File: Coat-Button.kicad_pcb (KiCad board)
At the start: 2 copper layers, 18 x 18 mm, 24 parts, among them IC1 MADW__ATTINY13-MM, P1 CONN_1, P2 CONN_1, P3 CONN_1, P4 CONN_1

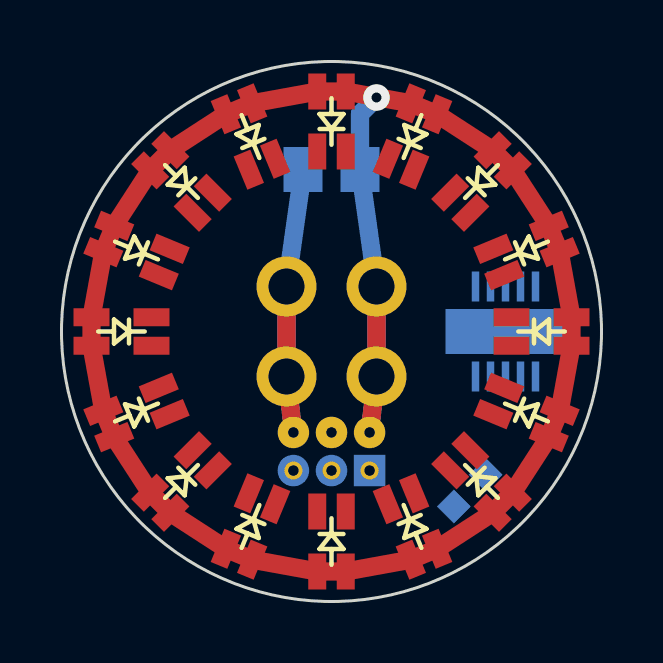
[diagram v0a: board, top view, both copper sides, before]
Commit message: On-board ATtiny13 wasn't doable. Not enough space.
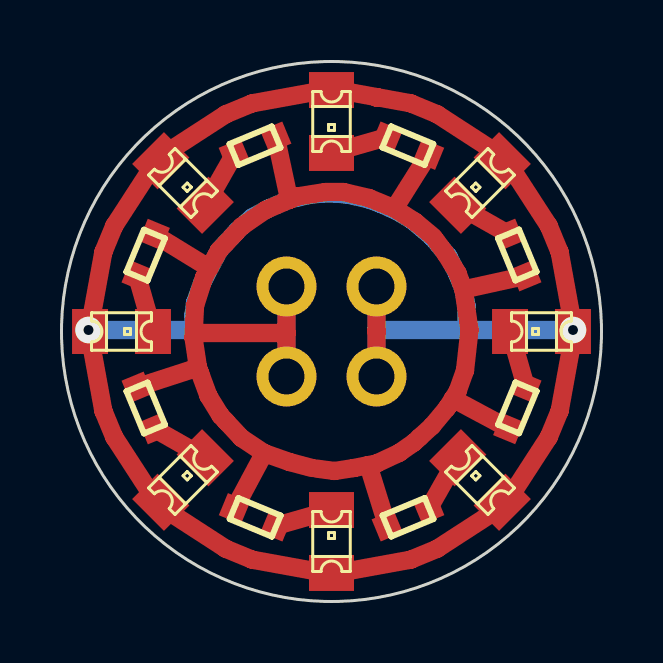
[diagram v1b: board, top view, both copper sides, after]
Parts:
- removed C1: 4.7µF, MADW__C0805
- removed IC1: MADW__ATTINY13-MM, MADW__MLF10
- removed JP1: AVR_ISP, MADW__PIN_ARRAY_3x2_1.27mm
- removed LED_A1_1, LED_A1_2, LED_A1_3, LED_A1_4, LED_A1_5, LED_A2_1, LED_A2_2, LED_A2_3, LED_A2_4, LED_A2_5, LED_B1_1, LED_B1_2, LED_B1_3, LED_B2_1, LED_B2_2, LED_B2_3: MADW__BI-LED, MADW__CHIPLED-0805-dual
- added D1: LED, MADW__CHIPLED-0805, F.Cu at (75.0, 55.0)
- added D2: LED, MADW__CHIPLED-0805, F.Cu at (75.0, 69.0)
- added D3: LED, MADW__CHIPLED-0805, F.Cu at (82.0, 62.0)
- added D4: LED, MADW__CHIPLED-0805, F.Cu at (68.0, 62.0)
- added D5: LED, MADW__CHIPLED-0805, F.Cu at (80.0, 57.0)
- added D6: LED, MADW__CHIPLED-0805, F.Cu at (80.0, 67.0)
- added D7: LED, MADW__CHIPLED-0805, F.Cu at (70.0, 67.0)
- added D8: LED, MADW__CHIPLED-0805, F.Cu at (70.0, 57.0)
- added G***: LED_smile_silkscreen_5mm, LED_smile_silkscreen_5mm, B.Cu at (75.0, 56.4)
- added G***: OSHW-logo_silkscreen_5mm, OSHW-logo_silkscreen_5mm, B.Cu at (75.0, 68.1)
- added R2: R, MADW__R0603, F.Cu at (72.5, 68.2)
- added R3: R, MADW__R0603, F.Cu at (81.2, 64.5)
- added R4: R, MADW__R0603, F.Cu at (68.8, 59.5)
- added R5: R, MADW__R0603, F.Cu at (81.2, 59.5)
- added R6: R, MADW__R0603, F.Cu at (77.5, 68.2)
- added R7: R, MADW__R0603, F.Cu at (68.8, 64.5)
- added R8: R, MADW__R0603, F.Cu at (72.5, 55.8)
- P1, P2, P4: footprint 1pin -> MADW__SIL-1
- R1: value 10k -> R; moved to F.Cu
- moved R1 11.7 mm to (77.5, 55.8), turned to 157.5 degrees
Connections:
- R1 pad 1: /RST -> GND
- R1 pad 2: VCC -> N-000009
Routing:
- net GND: track 13.7 -> 55.2 mm
- net VCC: track 66.8 -> 81.0 mm, vias 1 -> 2
- net N-000008: track 0.00 -> 1.95 mm
- net N-000007: track 0.00 -> 1.95 mm
- net N-000006: track 0.00 -> 1.95 mm
- net N-000005: track 0.00 -> 1.95 mm
- net N-000009: track 0.00 -> 1.93 mm
- net N-000002: track 0.00 -> 1.93 mm
- net N-000004: track 0.00 -> 1.93 mm
- net N-000003: track 0.00 -> 1.93 mm
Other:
- net class Default: via_dia 0.889 -> 0.635
- net class LED added: clearance 0.1524, trace_width 0.3048, via_dia 0.635, via_drill 0.3302
- rule via_min_size: 0.889 -> 0.635
- board text added: "+"
- board text added: "-"
- board text added: "2013"
- board text added: "blog. spitzenpfeil.org"

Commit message: Added some stuff to the 'Driver-Board'.
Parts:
- R1, R2, R3, R4, R5, R6, R7, R8: value R -> 200
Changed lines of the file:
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@@
     (links 26)
     (no_connects 0)
-    (area 62.564285 52.949999 84.357142 71.050001)
+    (area 65.949999 52.949999 84.050001 71.050001)
     (thickness 1.6)
     (drawings 8)
@@
       (effects (font (size 1 1) (thickness 0.2)))
     )
-    (fp_text value R (at 0.01 1.61 157.5) (layer F.SilkS) hide
+    (fp_text value 200 (at 0.01 1.61 157.5) (layer F.SilkS) hide
       (effects (font (size 1 1) (thickness 0.2)))
     )
@@
       (effects (font (size 1 1) (thickness 0.2)))
     )
-    (fp_text value R (at 0.01 1.61 337.5) (layer F.SilkS) hide
+    (fp_text value 200 (at 0.01 1.61 337.5) (layer F.SilkS) hide
       (effects (font (size 1 1) (thickness 0.2)))
     )
@@
       (effects (font (size 1 1) (thickness 0.2)))
     )
-    (fp_text value R (at 0.01 1.61 67.5) (layer F.SilkS) hide
+    (fp_text value 200 (at 0.01 1.61 67.5) (layer F.SilkS) hide
       (effects (font (size 1 1) (thickness 0.2)))
     )
@@
       (effects (font (size 1 1) (thickness 0.2)))
     )
-    (fp_text value R (at 0.01 1.61 247.5) (layer F.SilkS) hide
+    (fp_text value 200 (at 0.01 1.61 247.5) (layer F.SilkS) hide
       (effects (font (size 1 1) (thickness 0.2)))
     )
@@
       (effects (font (size 1 1) (thickness 0.2)))
     )
-    (fp_text value R (at 0.01 1.61 112.5) (layer F.SilkS) hide
+    (fp_text value 200 (at 0.01 1.61 112.5) (layer F.SilkS) hide
       (effects (font (size 1 1) (thickness 0.2)))
     )
@@
       (effects (font (size 1 1) (thickness 0.2)))
     )
-    (fp_text value R (at 0.01 1.61 22.5) (layer F.SilkS) hide
+    (fp_text value 200 (at 0.01 1.61 22.5) (layer F.SilkS) hide
       (effects (font (size 1 1) (thickness 0.2)))
     )
@@
       (effects (font (size 1 1) (thickness 0.2)))
     )
-    (fp_text value R (at 0.01 1.61 292.5) (layer F.SilkS) hide
+    (fp_text value 200 (at 0.01 1.61 292.5) (layer F.SilkS) hide
       (effects (font (size 1 1) (thickness 0.2)))
     )
@@
       (effects (font (size 1 1) (thickness 0.2)))
     )
-    (fp_text value R (at 0.01 1.61 202.5) (layer F.SilkS) hide
-      (effects (font (size 1 1) (thickness 0.2)))
-    )
+    (fp_text value 200 (at 0.01 1.61 202.5) (layer F.SilkS) hide
+      (effects (font (size 1 1) (thickness 0.2)))
+    )
